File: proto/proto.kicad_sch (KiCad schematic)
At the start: 2 parts, among them U1 ATmega32U4-M, Y1 CSTNE16M0V53C000R0

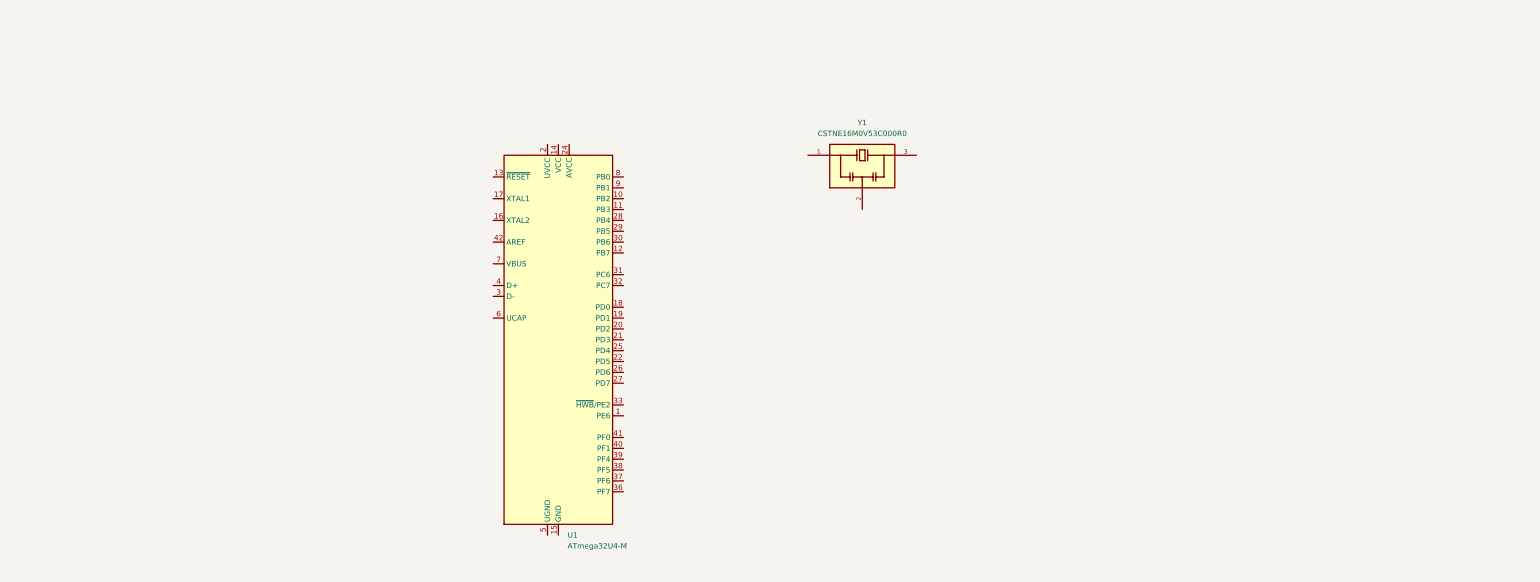
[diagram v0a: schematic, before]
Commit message: Add prototyping board (Rev 0)
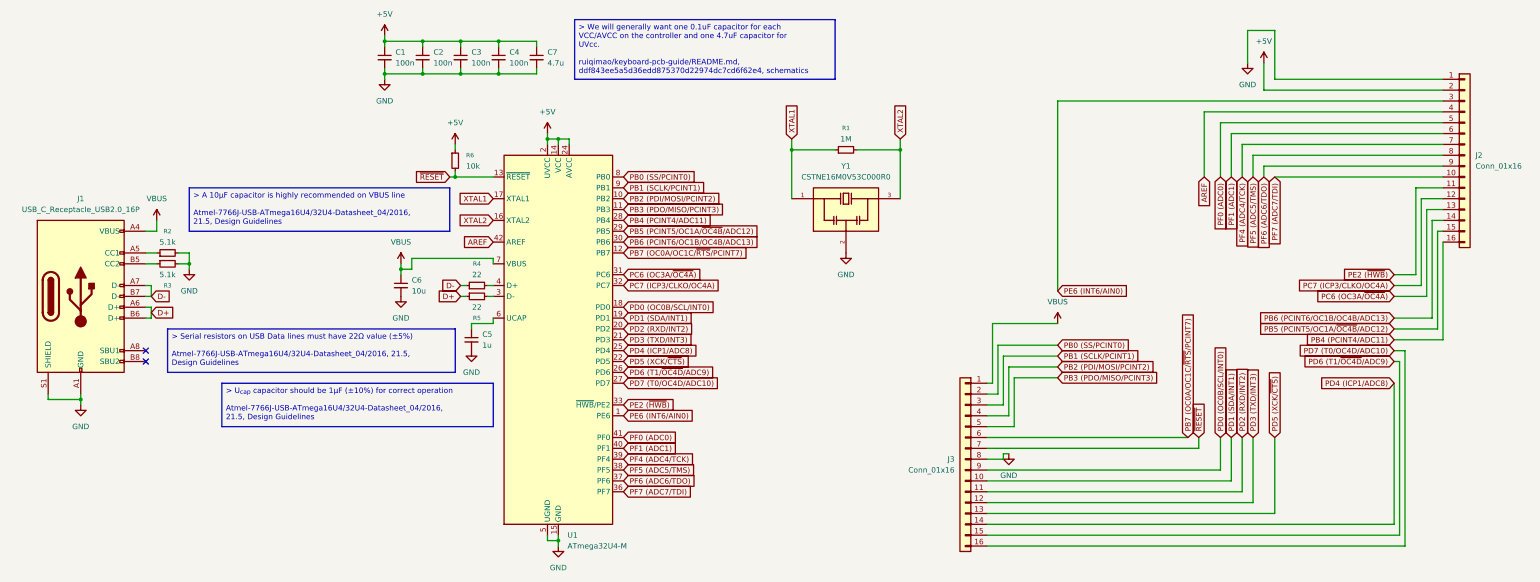
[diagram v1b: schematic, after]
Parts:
- added C1, C2, C3, C4: 100n, Capacitor_SMD:C_0402_1005Metric, symbol Device:C_Small
- added C5: 1u, Capacitor_SMD:C_0402_1005Metric, symbol Device:C_Small
- added C6: 10u, Capacitor_SMD:C_0402_1005Metric, symbol Device:C_Small
- added C7: 4.7u, Capacitor_SMD:C_0402_1005Metric, symbol Device:C_Small
- added J1: USB_C_Receptacle_USB2.0_16P, Connector_USB:USB_C_Receptacle_HRO_TYPE-C-31-M-12, symbol Connector:USB_C_Receptacle_USB2.0_16P
- added J2, J3: Conn_01x16, Connector_PinHeader_2.54mm:PinHeader_1x16_P2.54mm_Vertical, symbol Connector_Generic:Conn_01x16
- added R1: 1M, Resistor_SMD:R_0402_1005Metric, symbol Device:R_Small
- added R2, R3: 5.1k, Resistor_SMD:R_0402_1005Metric, symbol Device:R_Small
- added R4, R5: 22, Resistor_SMD:R_0402_1005Metric, symbol Device:R_Small
- added R6: 10k, Resistor_SMD:R_0402_1005Metric, symbol Device:R_Small
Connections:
- net PE6 (INT6/AIN0): now reaches U1.1 (PE6)
- net PE6 (INT6/AIN0): now also J2.3 (Pin_3)
- net PB2 (PDI/MOSI/PCINT2): now reaches U1.10 (PB2)
- net PB2 (PDI/MOSI/PCINT2): now also J3.4 (Pin_4)
- net PB3 (PDO/MISO/PCINT3): now reaches U1.11 (PB3)
- net PB3 (PDO/MISO/PCINT3): now also J3.5 (Pin_5)
- net PB7 (OC0A/OC1C/~{RTS}/PCINT7): now reaches U1.12 (PB7)
- net PB7 (OC0A/OC1C/~{RTS}/PCINT7): now also J3.6 (Pin_6)
- net ~{RESET}: now reaches U1.13 (~{RESET})
- net ~{RESET}: now also J3.7 (Pin_7), R6.2
- net +5V: now reaches U1.14 (VCC), U1.34 (VCC)
- net +5V: now also U1.2 (UVCC), U1.24 (AVCC), U1.44 (AVCC), C1.1, C2.1, C3.1, C4.1, C7.1, J2.2 (Pin_2), R6.1
- net GND: now reaches U1.15 (GND), U1.23 (GND), U1.35 (GND), U1.43 (GND), U1.45 (GND)
- net GND: now also U1.5 (UGND), Y1.2, C1.2, C2.2, C3.2, C4.2, C5.2, C6.2, C7.2, J1.A1 (GND), J1.A12 (GND), J1.B1 (GND), J1.B12 (GND), J1.S1 (SHIELD), J2.1 (Pin_1), J3.8 (Pin_8), R2.2, R3.2
- net XTAL2: now reaches U1.16 (XTAL2)
- net XTAL2: now also Y1.3, R1.2
- net XTAL1: now reaches U1.17 (XTAL1)
- net XTAL1: now also Y1.1, R1.1
- net PD0 (OC0B/SCL/INT0): now reaches U1.18 (PD0)
- net PD0 (OC0B/SCL/INT0): now also J3.9 (Pin_9)
- net PD1 (SDA/INT1): now reaches U1.19 (PD1)
- net PD1 (SDA/INT1): now also J3.10 (Pin_10)
- net PD2 (RXD/INT2): now reaches U1.20 (PD2)
- net PD2 (RXD/INT2): now also J3.11 (Pin_11)
- net PD3 (TXD/INT3): now reaches U1.21 (PD3)
- net PD3 (TXD/INT3): now also J3.12 (Pin_12)
- net PD5 (XCK/~{CTS}): now reaches U1.22 (PD5)
- net PD5 (XCK/~{CTS}): now also J3.13 (Pin_13)
- net PD4 (ICP1/ADC8): now reaches U1.25 (PD4)
- net PD4 (ICP1/ADC8): now also J3.14 (Pin_14)
- net PD6 (T1/~{OC4D}/ADC9): now reaches U1.26 (PD6)
- net PD6 (T1/~{OC4D}/ADC9): now also J3.15 (Pin_15)
- net PD7 (T0/OC4D/ADC10): now reaches U1.27 (PD7)
- net PD7 (T0/OC4D/ADC10): now also J3.16 (Pin_16)
- net PB4 (PCINT4/ADC11): now reaches U1.28 (PB4)
- net PB4 (PCINT4/ADC11): now also J2.16 (Pin_16)
- net PB5 (PCINT5/OC1A/~{OC4B}/ADC12): now reaches U1.29 (PB5)
- net PB5 (PCINT5/OC1A/~{OC4B}/ADC12): now also J2.15 (Pin_15)
- net at U1.3 (D-): now also R5.2
- net PB6 (PCINT6/OC1B/OC4B/ADC13): now reaches U1.30 (PB6)
- net PB6 (PCINT6/OC1B/OC4B/ADC13): now also J2.14 (Pin_14)
- net PC6 (OC3A/~{OC4A}): now reaches U1.31 (PC6)
- net PC6 (OC3A/~{OC4A}): now also J2.13 (Pin_13)
- net PC7 (ICP3/CLKO/OC4A): now reaches U1.32 (PC7)
- net PC7 (ICP3/CLKO/OC4A): now also J2.12 (Pin_12)
- net PE2 (~{HWB}): now reaches U1.33 (~{HWB}/PE2)
- net PE2 (~{HWB}): now also J2.11 (Pin_11)
- net PF7 (ADC7/TDI): now reaches U1.36 (PF7)
- net PF7 (ADC7/TDI): now also J2.10 (Pin_10)
- net PF6 (ADC6/TDO): now reaches U1.37 (PF6)
- net PF6 (ADC6/TDO): now also J2.9 (Pin_9)
- net PF5 (ADC5/TMS): now reaches U1.38 (PF5)
- net PF5 (ADC5/TMS): now also J2.8 (Pin_8)
- net PF4 (ADC4/TCK): now reaches U1.39 (PF4)
- net PF4 (ADC4/TCK): now also J2.7 (Pin_7)
- net at U1.4 (D+): now also R4.2
- net PF1 (ADC1): now reaches U1.40 (PF1)
- net PF1 (ADC1): now also J2.6 (Pin_6)
- net PF0 (ADC0): now reaches U1.41 (PF0)
- net PF0 (ADC0): now also J2.5 (Pin_5)
- net AREF: now reaches U1.42 (AREF)
- net AREF: now also J2.4 (Pin_4)
- net at U1.6 (UCAP): now also C5.1
- net VBUS: now reaches U1.7 (VBUS)
- net VBUS: now also C6.1, J1.A4 (VBUS), J1.A9 (VBUS), J1.B4 (VBUS), J1.B9 (VBUS), J3.1 (Pin_1)
- net PB0 (SS/PCINT0): now reaches U1.8 (PB0)
- net PB0 (SS/PCINT0): now also J3.2 (Pin_2)
- net PB1 (SCLK/PCINT1): now reaches U1.9 (PB1)
- net PB1 (SCLK/PCINT1): now also J3.3 (Pin_3)
- new net: J1.B5 (CC2), R3.1
- new net: J1.A5 (CC1), R2.1
- new net D+: J1.A6 (D+), J1.B6 (D+), R5.1
- new net D-: J1.A7 (D-), J1.B7 (D-), R4.1
- no-connect marks 0 -> 2
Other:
- moved on the sheet: Y1
